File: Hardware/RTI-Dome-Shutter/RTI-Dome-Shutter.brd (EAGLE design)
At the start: 80 x 71.1 mm, 42 parts, among them IC1 24AA128ST, IC5 74LVC245, IC6 74ABT245, J1 POWERPOLE_POWER45A

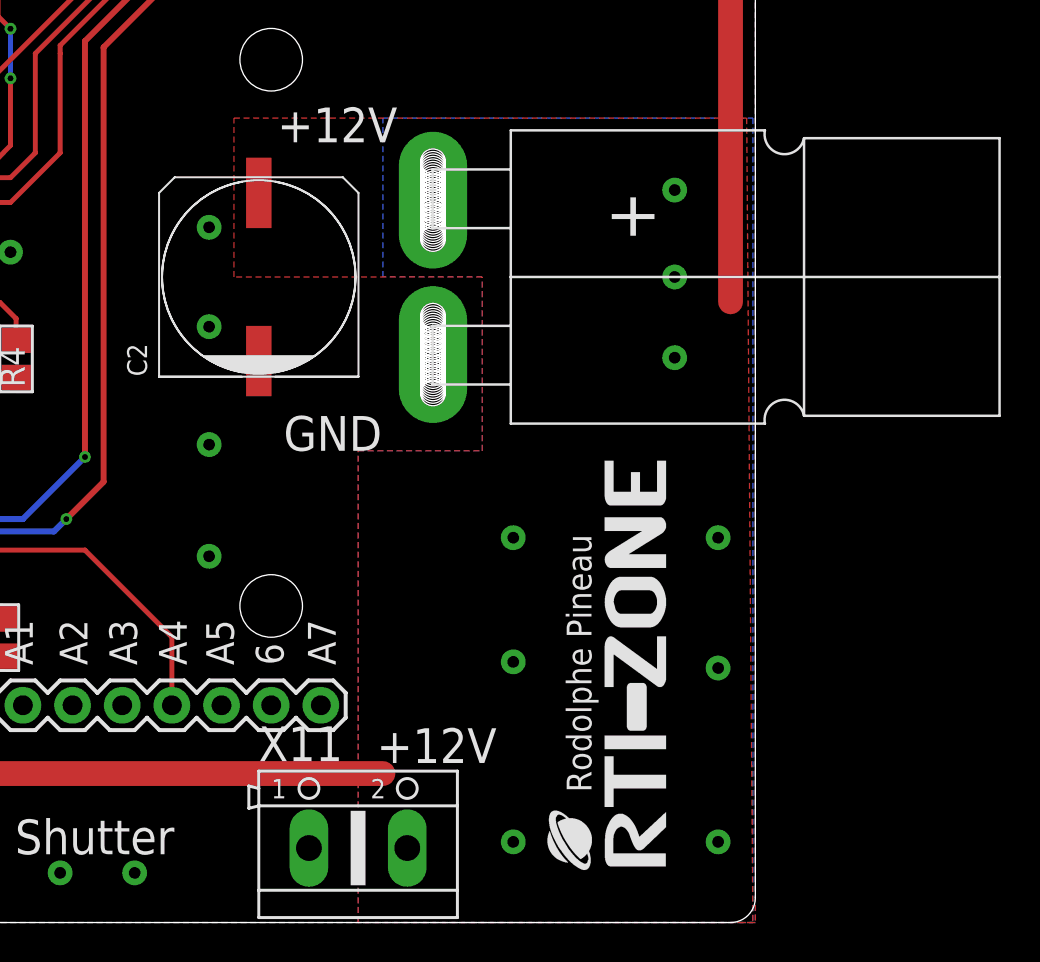
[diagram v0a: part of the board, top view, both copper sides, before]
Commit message: Started working on a new version using the Raspberry Pi RP2040 as a future replacement for the Arduino DUE
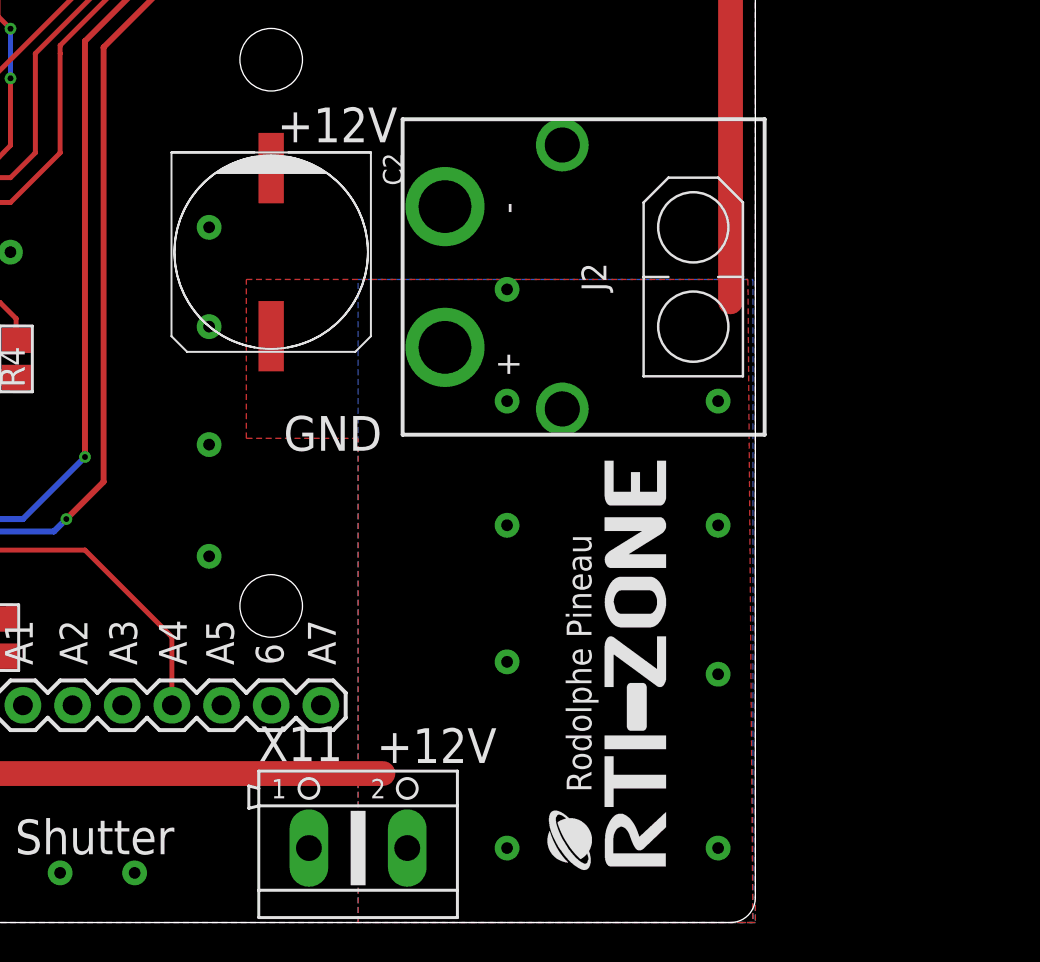
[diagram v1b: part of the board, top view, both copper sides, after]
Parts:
- removed J1: POWERPOLE_POWER45A, powerpoles:POWERPOLE_PAIR_45A
- added J2: XT60PW-M, samacsys:XT60PWM
- moved C2 1.42 mm to (55.2, 34.3), turned to 270 degrees
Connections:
- net +12V: now also J2.2; no longer J1.RED
- net GND: now also J2.1; no longer J1.BLACK
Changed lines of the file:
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@@
 <setting verticaltext="up"/>
 </settings>
-<grid distance="0.635" unitdist="mm" unit="mm" style="lines" multiple="1" display="yes" altdistance="0.03175" altunitdist="mm" altunit="mm"/>
+<grid distance="0.635" unitdist="mm" unit="mm" style="lines" multiple="1" display="yes" altdistance="0.127" altunitdist="mm" altunit="mm"/>
 <layers>
 <layer number="1" name="Top" color="4" fill="1" visible="yes" active="yes"/>
 <layer number="2" name="Route2" color="1" fill="3" visible="no" active="no"/>
 <layer number="3" name="Route3" color="4" fill="3" visible="no" active="no"/>
+<layer number="4" name="Route4" color="18" fill="4" visible="no" active="no"/>
+<layer number="5" name="Route5" color="19" fill="4" visible="no" active="no"/>
+<layer number="6" name="Route6" color="25" fill="8" visible="no" active="no"/>
+<layer number="7" name="Route7" color="26" fill="8" visible="no" active="no"/>
+<layer number="8" name="Route8" color="27" fill="2" visible="no" active="no"/>
+<layer number="9" name="Route9" color="28" fill="2" visible="no" active="no"/>
+<layer number="10" name="Route10" color="29" fill="7" visible="no" active="no"/>
+<layer number="11" name="Route11" color="30" fill="7" visible="no" active="no"/>
+<layer number="12" name="Route12" color="20" fill="5" visible="no" active="no"/>
+<layer number="13" name="Route13" color="21" fill="5" visible="no" active="no"/>
 <layer number="14" name="Route14" color="1" fill="6" visible="no" active="no"/>
 <layer number="15" name="Route15" color="4" fill="6" visible="no" active="no"/>
@@
 </element>
 <element name="U$4" library="rti" package="LOGO_BIG" value="RTI-LOGO_BIG" x="75.438" y="2.8575" smashed="yes" rot="R90"/>
-<element name="C2" library="rti" package="UD-10X10_NICHICON" value="100uF" x="54.61" y="33.02" smashed="yes" rot="R90">
-<attribute name="NAME" x="48.895" y="27.94" size="1.016" layer="25" rot="R90"/>
-<attribute name="VALUE" x="60.96" y="27.94" size="1.016" layer="27" rot="R90"/>
+<element name="C2" library="rti" package="UD-10X10_NICHICON" value="100uF" x="55.245" y="34.29" smashed="yes" rot="R270">
+<attribute name="NAME" x="60.96" y="39.37" size="1.016" layer="25" rot="R270"/>
+<attribute name="VALUE" x="48.895" y="39.37" size="1.016" layer="27" rot="R270"/>
 </element>
 <element name="R13" library="rti" package="R0805" value="4.7K" x="5.08" y="20.3835" smashed="yes" rot="R180">
@@
 <attribute name="VALUE" x="9.91" y="21.705" size="0.8128" layer="27" font="vector" rot="R270"/>
 </element>
-<element name="J1" library="powerpoles" package="POWERPOLE_PAIR_45A" value="POWERPOLE_POWER45A" x="63.5" y="33.02" smashed="yes" rot="R270"/>
 <element name="U$1" library="MCP120T" package="SOT95P237X112-3N" value="MCP120T-315I/TT" x="22.86" y="15.24" smashed="yes">
 <attribute name="DESCRIPTION" value="Microcontroller Supervisory Circuit" x="22.86" y="15.24" size="1.778" layer="27" display="off"/>
@@
 <attribute name="NAME" x="3.175" y="53.34" size="1.27" layer="25" rot="R180"/>
 <attribute name="VALUE" x="3.175" y="57.15" size="1.27" layer="27" rot="R180"/>
+</element>
+<element name="J2" library="samacsys" library_urn="urn:adsk.eagle:library:37256869" package="XT60PWM" package3d_urn="urn:adsk.eagle:package:37256940/5" value="XT60PW-M" x="64.135" y="33.02" smashed="yes" rot="R270">
+<attribute name="ARROW_PART_NUMBER" value="" x="64.135" y="33.02" size="1.778" layer="27" rot="R270" display="off"/>
+<attribute name="ARROW_PRICE-STOCK" value="" x="64.135" y="33.02" size="1.778" layer="27" rot="R270" display="off"/>
+<attribute name="DESCRIPTION" value="Socket; DC supply; XT60; male; PIN: 2; on PCBs; THT; Colour: yellow" x="64.135" y="33.02" size="1.778" layer="27" rot="R270" display="off"/>
+<attribute name="HEIGHT" value="8.4mm" x="64.135" y="33.02" size="1.778" layer="27" rot="R270" display="off"/>
+<attribute name="MANUFACTURER_NAME" value="Changzou Amass Elec" x="64.135" y="33.02" size="1.778" layer="27" rot="R270" display="off"/>
+<attribute name="MANUFACTURER_PART_NUMBER" value="XT60PW-M" x="64.135" y="33.02" size="1.778" layer="27" rot="R270" display="off"/>
+<attribute name="MOUSER_PART_NUMBER" value="" x="64.135" y="33.02" size="1.778" layer="27" rot="R270" display="off"/>
+<attribute name="MOUSER_PRICE-STOCK" value="" x="64.135" y="33.02" size="1.778" layer="27" rot="R270" display="off"/>
+<attribute name="MOUSER_TESTING_PART_NUMBER" value="" x="64.135" y="33.02" size="1.778" layer="27" rot="R270" display="off"/>
+<attribute name="MOUSER_TESTING_PRICE-STOCK" value="" x="64.135" y="33.02" size="1.778" layer="27" rot="R270" display="off"/>
+<attribute name="NAME" x="71.755" y="33.02" size="1.27" layer="25" rot="R270" align="center"/>
+<attribute name="VALUE" x="69.215" y="33.02" size="1.27" layer="27" rot="R270" align="center"/>
 </element>
 </elements>
@@
 <contactref element="IC6" pad="P$19"/>
 <via x="37.17925" y="35.052" extent="1-16" drill="0.3" diameter="0.254"/>
-<contactref element="J1" pad="BLACK"/>
 <contactref element="U$1" pad="3"/>
 <contactref element="IC5" pad="P$19"/>
@@
 <via x="12.7" y="18.0975" extent="1-16" drill="0.6" diameter="1.27"/>
 <contactref element="IC5" pad="P$9"/>
+<contactref element="J2" pad="1"/>
 </signal>
 <signal name="+12V" class="1">
@@
 <contactref element="C2" pad="+"/>
 <polygon width="0.3048" layer="1" thermals="no">
-<vertex x="53.34" y="41.148"/>
-<vertex x="79.5655" y="41.148"/>
+<vertex x="53.975" y="32.893"/>
+<vertex x="79.629196875" y="32.893"/>
 <vertex x="79.883" y="0"/>
 <vertex x="59.69" y="0"/>
-<vertex x="59.69" y="24.13"/>
-<vertex x="66.04" y="24.13"/>
-<vertex x="66.04" y="33.02"/>
-<vertex x="53.34" y="33.02"/>
+<vertex x="59.69" y="24.765"/>
+<vertex x="53.975" y="24.765"/>
 </polygon>
 <contactref element="R10" pad="2"/>
@@
 <wire x1="25.4" y1="69.85" x2="23.83155" y2="68.40855" width="1.27" layer="1" curve="90"/>
 <polygon width="0.254" layer="16" thermals="no">
-<vertex x="60.96" y="41.148"/>
-<vertex x="79.883" y="41.148"/>
+<vertex x="59.69" y="32.893"/>
+<vertex x="79.883" y="32.893"/>
 <vertex x="79.883" y="0"/>
 <vertex x="59.69" y="0"/>
-<vertex x="59.69" y="24.13"/>
-<vertex x="66.04" y="24.13"/>
-<vertex x="66.04" y="33.02"/>
-<vertex x="60.96" y="33.02"/>
 </polygon>
 <wire x1="34.9225" y1="13.5255" x2="34.925" y2="13.5255" width="0.8128" layer="1"/>
 <wire x1="34.925" y1="13.5255" x2="34.925" y2="11.1125" width="0.8128" layer="1"/>
-<contactref element="J1" pad="RED"/>
 <wire x1="34.925" y1="11.1125" x2="36.83" y2="7.62" width="1.27" layer="1"/>
 <wire x1="36.83" y1="7.62" x2="60.96" y2="7.62" width="1.27" layer="1"/>
 <wire x1="34.925" y1="8.697" x2="34.925" y2="11.1125" width="1.27" layer="1"/>
-<via x="75.8825" y="37.465" extent="1-16" drill="0.6" diameter="1.27"/>
-<via x="75.8825" y="33.02" extent="1-16" drill="0.6" diameter="1.27"/>
-<via x="75.8825" y="28.8925" extent="1-16" drill="0.6" diameter="1.27"/>
-<via x="78.105" y="19.685" extent="1-16" drill="0.6" diameter="1.27"/>
-<via x="78.105" y="13.0175" extent="1-16" drill="0.6" diameter="1.27"/>
-<via x="78.105" y="4.1275" extent="1-16" drill="0.6" diameter="1.27"/>
-<via x="67.6275" y="19.685" extent="1-16" drill="0.6" diameter="1.27"/>
-<via x="67.6275" y="13.335" extent="1-16" drill="0.6" diameter="1.27"/>
-<via x="67.6275" y="4.1275" extent="1-16" drill="0.6" diameter="1.27"/>
+<via x="67.31" y="32.385" extent="1-16" drill="0.6" diameter="1.27"/>
+<via x="67.31" y="26.67" extent="1-16" drill="0.6" diameter="1.27"/>
+<via x="78.105" y="26.67" extent="1-16" drill="0.6" diameter="1.27"/>
+<via x="78.105" y="20.32" extent="1-16" drill="0.6" diameter="1.27"/>
+<via x="78.105" y="12.7" extent="1-16" drill="0.6" diameter="1.27"/>
+<via x="78.105" y="3.81" extent="1-16" drill="0.6" diameter="1.27"/>
+<via x="67.31" y="20.32" extent="1-16" drill="0.6" diameter="1.27"/>
+<via x="67.31" y="13.335" extent="1-16" drill="0.6" diameter="1.27"/>
+<via x="67.31" y="3.81" extent="1-16" drill="0.6" diameter="1.27"/>
+<contactref element="J2" pad="2"/>
 </signal>
 <signal name="SHUTTER_OPENED">
@@
 </board>
 </drawing>
+<compatibility>
+<note version="8.2" severity="warning">
+Since Version 8.2, EAGLE supports online libraries. The ids
+of those online libraries will not be understood (or retained)
+with this version.
+</note>
+<note version="8.3" severity="warning">
+Since Version 8.3, EAGLE supports URNs for individual library
+assets (packages, symbols, and devices). The URNs of those assets
+will not be understood (or retained) with this version.
+</note>
+<note version="8.3" severity="warning">
+Since Version 8.3, EAGLE supports the association of 3D packages
+with devices in libraries, schematics, and board files. Those 3D
+packages will not be understood (or retained) with this version.
+</note>
+</compatibility>
 </eagle>
